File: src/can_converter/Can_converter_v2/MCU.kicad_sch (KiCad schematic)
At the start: 8 parts, among them J102 IDC6, U1 STM32G0B1CBT, Y1 830108313809

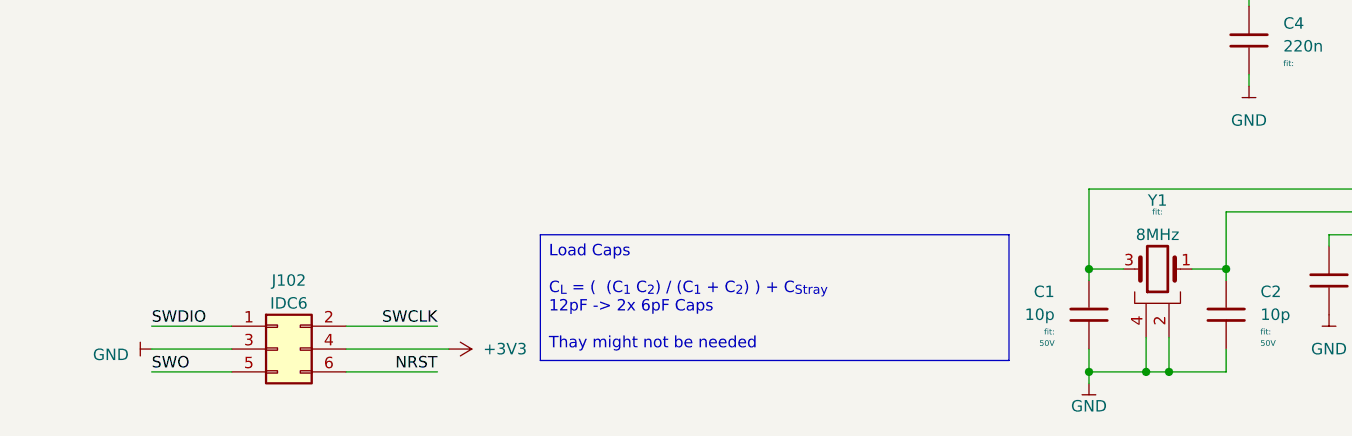
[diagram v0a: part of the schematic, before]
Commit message: Rebase usb-can branch onto main
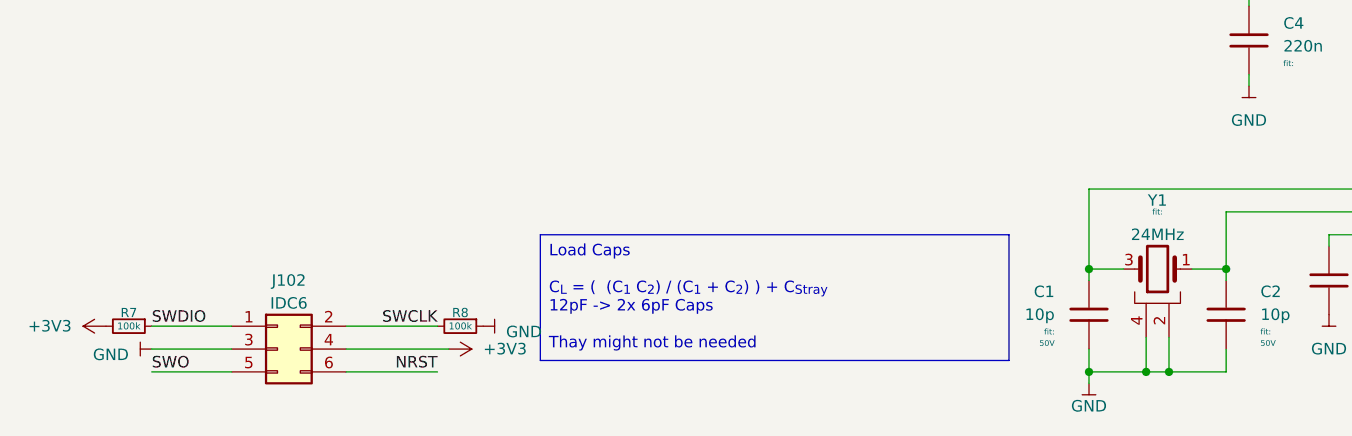
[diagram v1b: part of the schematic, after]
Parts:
- added R7, R8: 100k, Resistor_SMD:R_0402_1005Metric, symbol Bluesat:R_CompactV
- Y1: footprint Crystal:Crystal_SMD_Abracon_ABM8AIG-4Pin_3.2x2.5mm -> Crystal:Crystal_SMD_2016-4Pin_2.0x1.6mm; DisplayName 8MHz -> 24MHz
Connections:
- net +3V3: now also R7.2
- net GND: now also R8.1
- net SWCLK: now also R8.2
- net SWDIO: now also R7.1

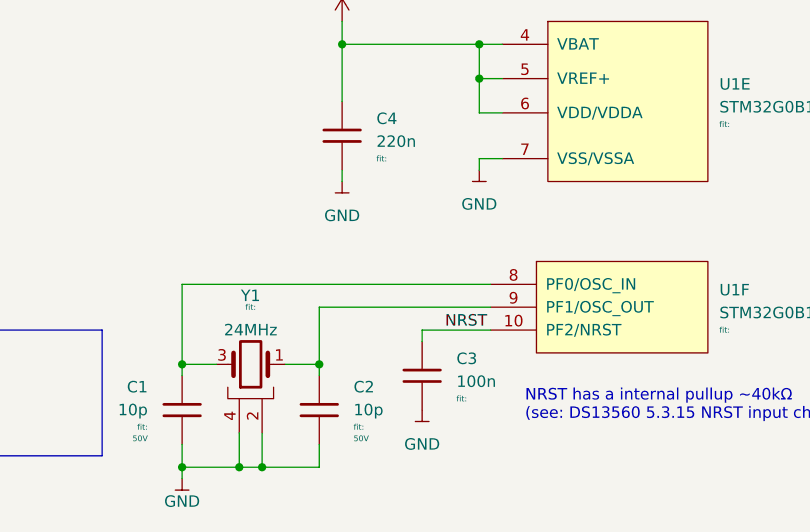
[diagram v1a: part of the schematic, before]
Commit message: Add 100R series on crystal oscillator
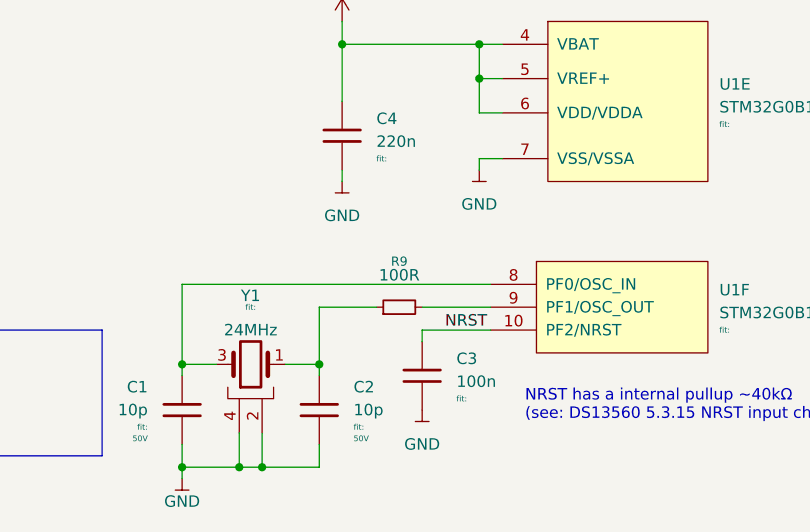
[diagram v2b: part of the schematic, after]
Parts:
- added R9: 100R, Resistor_SMD:R_0402_1005Metric, symbol Device:R_Small
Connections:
- net at C2.2, Y1.1 (C_{1}): now also R9.1; no longer U1.9 (PF1/OSC_OUT)
- new net: R9.2, U1.9 (PF1/OSC_OUT)
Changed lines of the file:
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@@
+	(wire
+		(pts
+			(xy 142.24 105.41) (xy 148.59 105.41)
+		)
+		(stroke
+			(width 0)
+			(type default)
+		)
+	)
 	(wire
 		(pts
@@
 	(wire
 		(pts
+			(xy 153.67 105.41) (xy 161.29 105.41)
+		)
+		(stroke
+			(width 0)
+			(type default)
+		)
+	)
+	(wire
+		(pts
 			(xy 144.78 73.66) (xy 144.78 76.2)
-		)
-		(stroke
-			(width 0)
-			(type default)
-		)
-	)
-	(wire
-		(pts
-			(xy 142.24 105.41) (xy 161.29 105.41)
 		)
 		(stroke
@@
 					(unit 1)
 				)
+			)
+		)
+	)
+	(symbol
+		(lib_id "Device:R_Small")
+		(at 151.13 105.41 90)
+		(unit 1)
+		(exclude_from_sim no)
+		(in_bom yes)
+		(on_board yes)
+		(dnp no)
+		(property "Reference" "R9"
+			(at 151.13 100.33 90)
+			(effects
+				(font
+					(size 1.016 1.016)
+				)
+			)
+		)
+		(property "Value" "100R"
+			(at 151.13 101.854 90)
+			(effects
+				(font
+					(size 1.27 1.27)
+				)
+			)
+		)
+		(property "Footprint" "Resistor_SMD:R_0402_1005Metric"
+			(at 151.13 105.41 0)
+			(effects
+				(font
+					(size 1.27 1.27)
+				)
+				(hide yes)
+			)
+		)
+		(property "Datasheet" "~"
+			(at 151.13 105.41 0)
+			(effects
+				(font
+					(size 1.27 1.27)
+				)
+				(hide yes)
+			)
+		)
+		(property "Description" "Resistor, small symbol"
+			(at 151.13 105.41 0)
+			(effects
+				(font
+					(size 1.27 1.27)
+				)
+				(hide yes)
+			)
+		)
+		(pin "2"
+		)
+		(pin "1"
+		)
+		(instances
+			(project ""
+				(path "/e63e39d7-6ac0-4ffd-8aa3-1841a4541b55/c754f27f-d753-4109-9c59-639a39396c66"
+					(reference "R9")
+					(unit 1)
+				)
